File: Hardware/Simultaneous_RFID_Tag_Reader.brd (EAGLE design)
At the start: 77.5 x 53.3 mm, 37 parts, among them J2 FTDI, J3 JST, J4 U.FL, J5 Extra, J6 Screw Terminal, J7 GPIOs, U1 Nano, U2 TXB0104, U3 ESD Diode

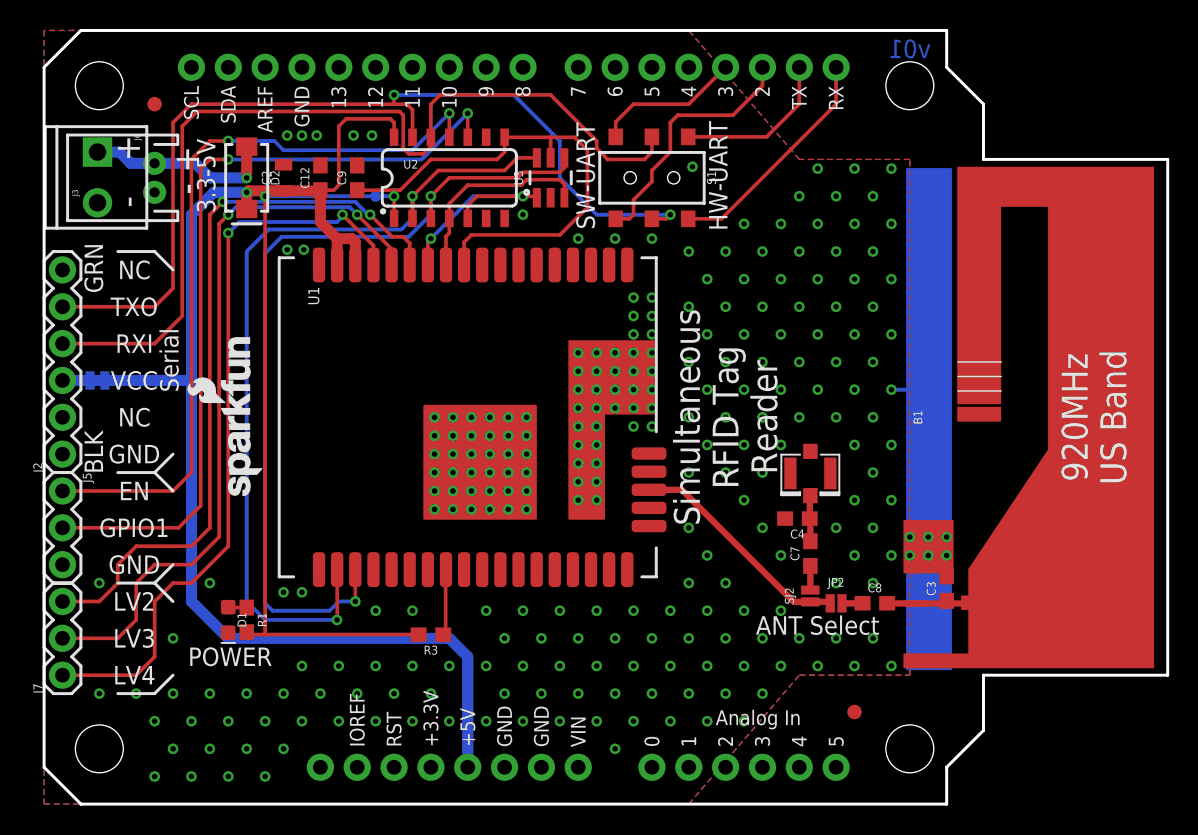
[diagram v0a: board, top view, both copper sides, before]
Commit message: Fixed problems found during review
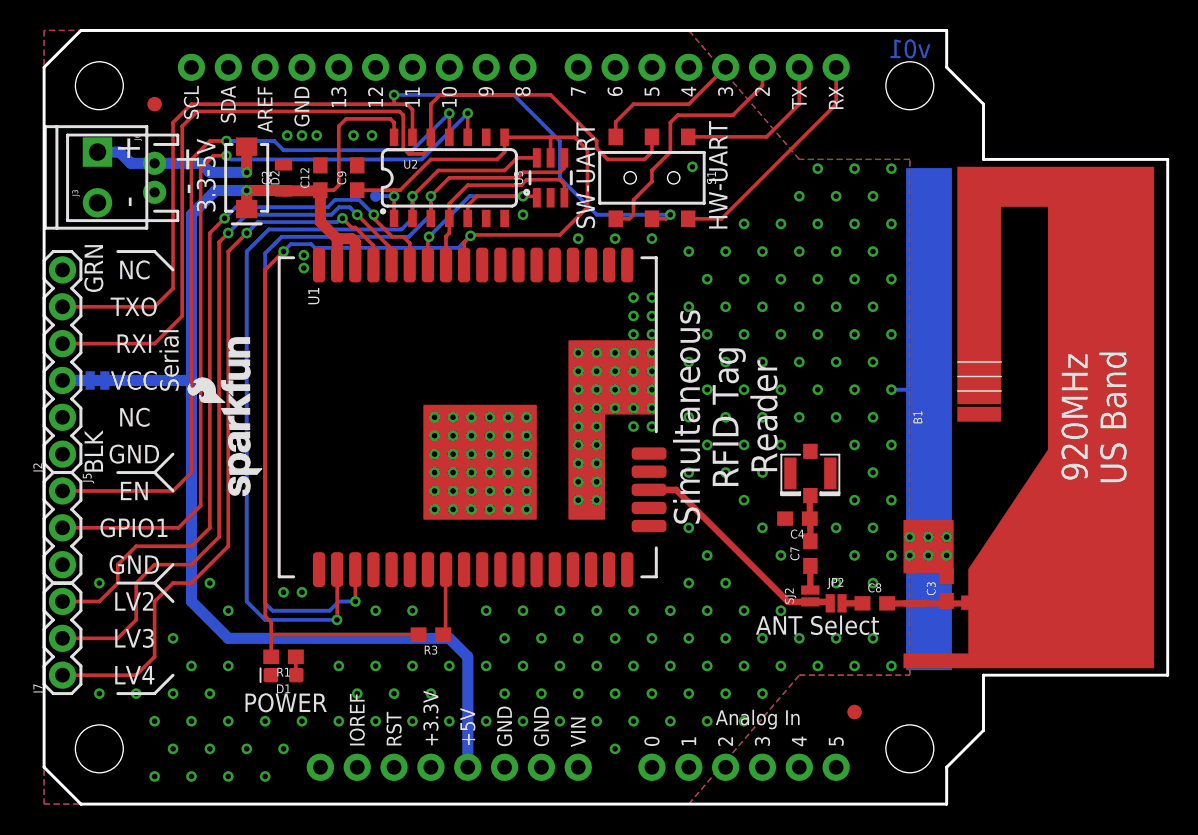
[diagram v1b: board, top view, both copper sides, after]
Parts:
- moved LOGO3 6.35 mm to (11.0, 21.0)
- moved D1 5.39 mm to (16.5, 8.89), turned to 180 degrees
- moved R1 3.59 mm to (16.5, 10.2), turned to 180 degrees
- turned LOGO2 to 90 degrees
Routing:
- net 3.3V: track 87.8 -> 90.4 mm, vias 2 -> 3
- net GPIO4-LV: track 51.8 -> 50.9 mm
- net GPIO3-LV: track 51.4 -> 50.7 mm
- net N$12: track 13.2 -> 12.6 mm
- net GND: track 9.50 -> 9.69 mm, vias 257 -> 256
